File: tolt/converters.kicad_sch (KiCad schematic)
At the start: 50 parts, among them U14 AMS1117-3.3, U15 LP5907MFX-3.3, U16 TPS62173DSG, U19 TLV61047DDC, U24 LTC7138xMSE

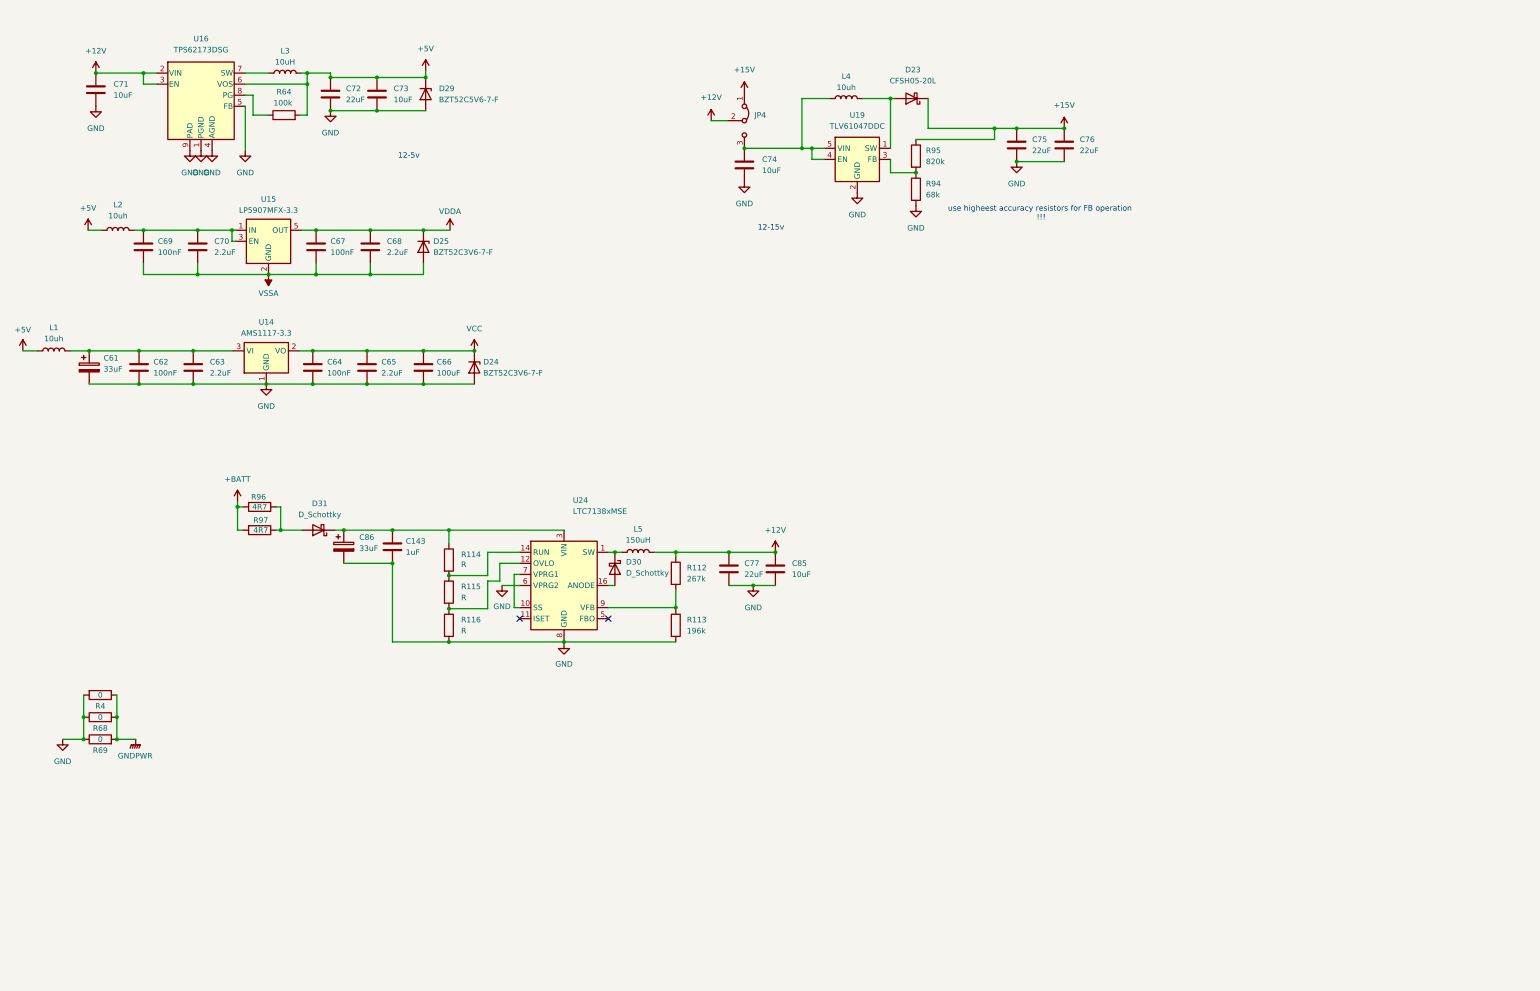
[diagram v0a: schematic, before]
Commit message: converter edit
2x ltc7137
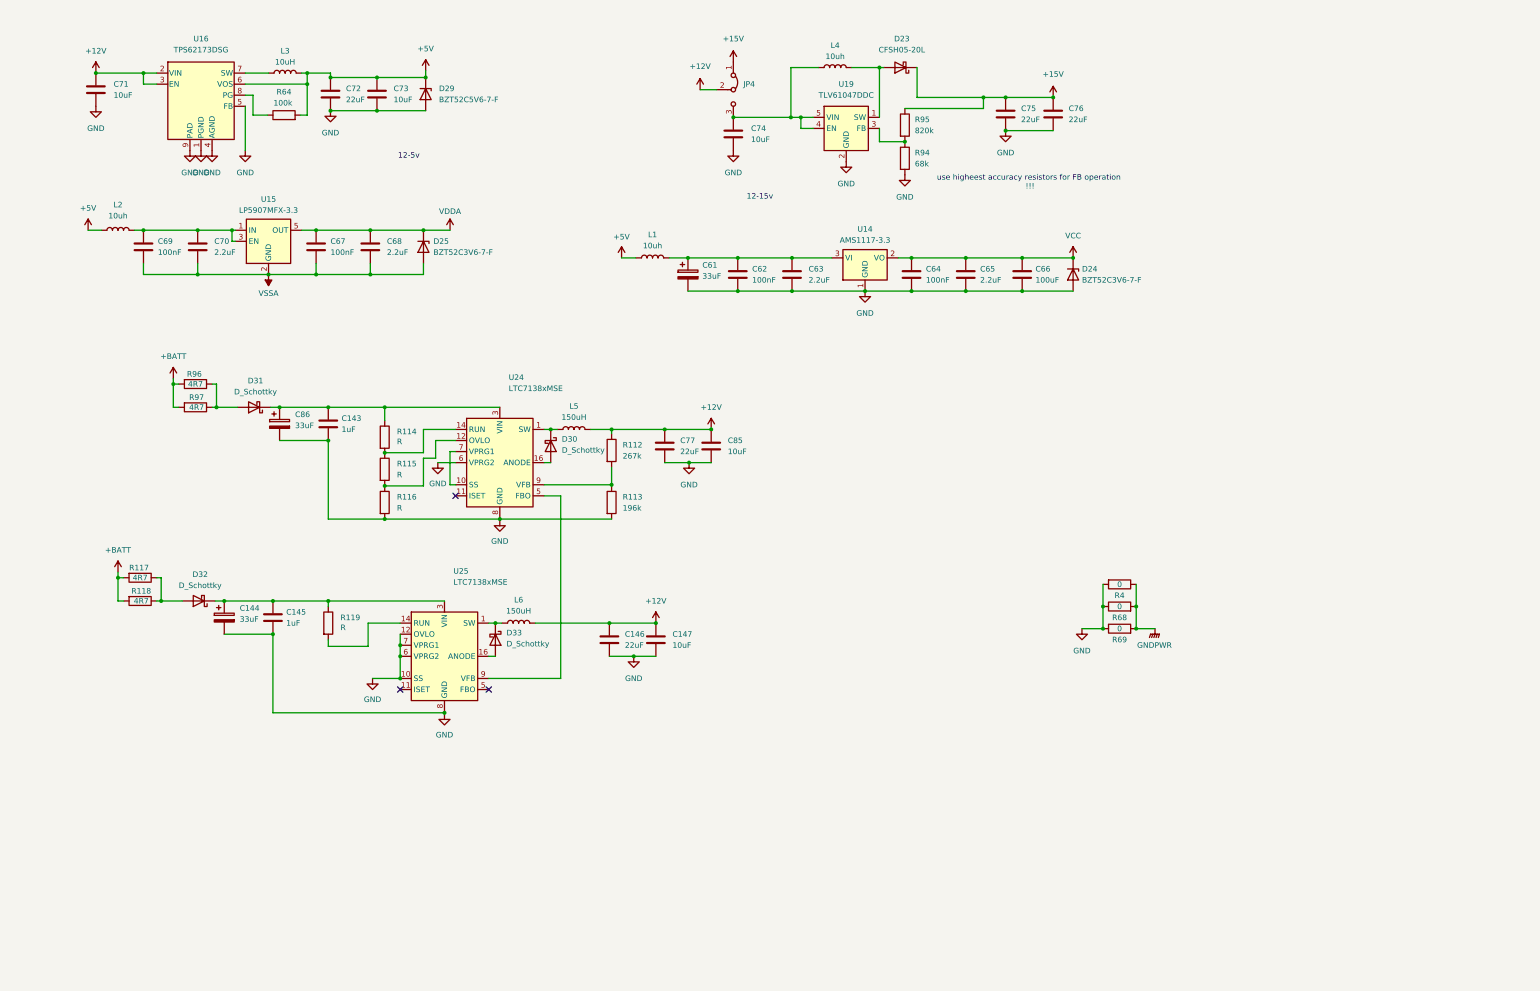
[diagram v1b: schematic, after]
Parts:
- added C144: 33uF, Capacitor_Tantalum_SMD:CP_EIA-3528-15_AVX-H, symbol Device:C_Polarized
- added C145: 1uF, Capacitor_SMD:C_2220_5750Metric, symbol Device:C
- added C146: 22uF, Capacitor_SMD:C_1210_3225Metric, symbol Device:C
- added C147: 10uF, Capacitor_SMD:C_1210_3225Metric, symbol Device:C
- added D32, D33: D_Schottky, symbol Device:D_Schottky
- added L6: 150uH, symbol Device:L
- added R117, R118: 4R7, Resistor_SMD:R_0805_2012Metric, symbol Device:R
- added R119: R, symbol Device:R
- added U25: LTC7138xMSE, Package_SO:Analog_MSOP-12-16-1EP_3x4.039mm_P0.5mm_EP1.651x2.845mm, symbol Regulator_Switching:LTC7138xMSE
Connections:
- net +12V: now also C146.2, C147.2, L6.2
- net +BATT: now also R117.2, R118.2
- net GND: now also C144.2, C145.2, C146.1, C147.1, U25.10 (SS), U25.12 (OVLO), U25.17 (GND), U25.6 (VPRG2), U25.7 (VPRG1), U25.8 (GND)
- net at U24.5 (FBO): now also U25.9 (VFB)
- new net: C144.1, C145.1, D32.1 (K), R119.1, U25.3 (VIN)
- new net: R119.2, U25.14 (RUN)
- new net: D32.2 (A), R117.1, R118.1
- new net: D33.1 (K), L6.1, U25.1 (SW)
- new net: D33.2 (A), U25.16 (ANODE)
- no-connect marks 2 -> 3
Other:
- moved on the sheet: C143, C61, C62, C63, C64, C65, C66, C74, C75, C76, C77, C85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

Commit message: more changes
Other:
- note added: "analog"
- note added: "consider using another converter for 15v ?"
- note added: "digital"
- note added: "dual 12v coneverter for 800ma output"
- moved on the sheet: R4, R68, R69
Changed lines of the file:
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@@
 		)
 	)
+	(text "analog\n"
+		(exclude_from_sim no)
+		(at 106.172 80.518 0)
+		(effects
+			(font
+				(size 1.27 1.27)
+			)
+		)
+	)
+	(text "consider using another converter for 15v ?"
+		(exclude_from_sim no)
+		(at 253.746 48.768 0)
+		(effects
+			(font
+				(size 1.27 1.27)
+			)
+		)
+	)
+	(text "dual 12v coneverter for 800ma output \n"
+		(exclude_from_sim no)
+		(at 149.606 183.134 0)
+		(effects
+			(font
+				(size 1.27 1.27)
+			)
+		)
+	)
 	(text "12-5v\n"
 		(exclude_from_sim no)
@@
 		)
 	)
+	(text "digital\n"
+		(exclude_from_sim no)
+		(at 259.588 84.836 0)
+		(effects
+			(font
+				(size 1.27 1.27)
+			)
+		)
+	)
 	(junction
 		(at 222.758 69.85)
@@
 	)
 	(junction
-		(at 266.7 149.86)
+		(at 241.3 127)
 		(diameter 0)
 		(color 0 0 0 0)
@@
 	)
 	(junction
-		(at 274.32 154.94)
+		(at 248.92 132.08)
 		(diameter 0)
 		(color 0 0 0 0)
@@
 	)
 	(junction
-		(at 274.32 149.86)
+		(at 248.92 127)
 		(diameter 0)
 		(color 0 0 0 0)
 	)
 	(junction
-		(at 266.7 154.94)
+		(at 241.3 132.08)
 		(diameter 0)
 		(color 0 0 0 0)
@@
 	(wire
 		(pts
-			(xy 274.32 149.86) (xy 274.32 154.94)
+			(xy 248.92 127) (xy 248.92 132.08)
 		)
 		(stroke
@@
 	(wire
 		(pts
-			(xy 274.32 144.78) (xy 274.32 149.86)
+			(xy 248.92 121.92) (xy 248.92 127)
 		)
 		(stroke
@@
 	(wire
 		(pts
-			(xy 266.7 149.86) (xy 266.7 154.94)
+			(xy 241.3 127) (xy 241.3 132.08)
 		)
 		(stroke
@@
 	(wire
 		(pts
-			(xy 261.874 154.94) (xy 266.7 154.94)
+			(xy 236.474 132.08) (xy 241.3 132.08)
 		)
 		(stroke
@@
 	(wire
 		(pts
-			(xy 274.32 154.94) (xy 278.638 154.94)
+			(xy 248.92 132.08) (xy 253.238 132.08)
 		)
 		(stroke
@@
 	(wire
 		(pts
-			(xy 266.7 144.78) (xy 266.7 149.86)
+			(xy 241.3 121.92) (xy 241.3 127)
 		)
 		(stroke
@@
 	(symbol
 		(lib_id "power:GNDPWR")
-		(at 278.638 154.94 0)
+		(at 253.238 132.08 0)
 		(unit 1)
 		(exclude_from_sim no)
@@
 		(fields_autoplaced yes)
 		(property "Reference" "#PWR0217"
-			(at 278.638 160.02 0)
+			(at 253.238 137.16 0)
 			(effects
 				(font
@@
 		)
 		(property "Value" "GNDPWR"
-			(at 278.511 158.75 0)
+			(at 253.111 135.89 0)
 			(effects
 				(font
@@
 		)
 		(property "Footprint" ""
-			(at 278.638 156.21 0)
+			(at 253.238 133.35 0)
 			(effects
 				(font
@@
 		)
 		(property "Datasheet" ""
-			(at 278.638 156.21 0)
+			(at 253.238 133.35 0)
 			(effects
 				(font
@@
 		)
 		(property "Description" "Power symbol creates a global label with name \"GNDPWR\" , global ground"
-			(at 278.638 154.94 0)
+			(at 253.238 132.08 0)
 			(effects
 				(font
@@
 	(symbol
 		(lib_id "Device:R")
-		(at 270.51 149.86 90)
+		(at 245.11 127 90)
 		(unit 1)
 		(exclude_from_sim no)
@@
 		(dnp no)
 		(property "Reference" "R68"
-			(at 270.51 152.4 90)
+			(at 245.11 129.54 90)
 			(effects
 				(font
@@
 		)
 		(property "Value" "0"
-			(at 270.51 149.86 90)
+			(at 245.11 127 90)
 			(effects
 				(font
@@
 		)
 		(property "Footprint" "Resistor_SMD:R_0815_2038Metric"
-			(at 270.51 151.638 90)
+			(at 245.11 128.778 90)
 			(effects
 				(font
@@
 		)
 		(property "Datasheet" "~"
-			(at 270.51 149.86 0)
+			(at 245.11 127 0)
 			(effects
 				(font
@@
 		)
 		(property "Description" "Resistor"
-			(at 270.51 149.86 0)
+			(at 245.11 127 0)
 			(effects
 				(font
@@
 	(symbol
 		(lib_id "power:GND")
-		(at 261.874 154.94 0)
+		(at 236.474 132.08 0)
 		(unit 1)
 		(exclude_from_sim no)
@@
 		(fields_autoplaced yes)
 		(property "Reference" "#PWR0218"
-			(at 261.874 161.29 0)
+			(at 236.474 138.43 0)
 			(effects
 				(font
@@
 		)
 		(property "Value" "GND"
-			(at 261.874 160.02 0)
+			(at 236.474 137.16 0)
 			(effects
 				(font
@@
 		)
 		(property "Footprint" ""
-			(at 261.874 154.94 0)
+			(at 236.474 132.08 0)
 			(effects
 				(font
@@
 		)
 		(property "Datasheet" ""
-			(at 261.874 154.94 0)
+			(at 236.474 132.08 0)
 			(effects
 				(font
@@
 		)
 		(property "Description" ""
-			(at 261.874 154.94 0)
+			(at 236.474 132.08 0)
 			(effects
 				(font
@@
 	(symbol
 		(lib_id "Device:R")
-		(at 270.51 144.78 270)
+		(at 245.11 121.92 270)
 		(unit 1)
 		(exclude_from_sim no)
@@
 		(dnp no)
 		(property "Reference" "R4"
-			(at 270.51 147.32 90)
+			(at 245.11 124.46 90)
 			(effects
 				(font
@@
 		)
 		(property "Value" "0"
-			(at 270.51 144.78 90)
+			(at 245.11 121.92 90)
 			(effects
 				(font
@@
 		)
 		(property "Footprint" "Resistor_SMD:R_0815_2038Metric"
-			(at 270.51 143.002 90)
+			(at 245.11 120.142 90)
 			(effects
 				(font
@@
 		)
 		(property "Datasheet" "~"
-			(at 270.51 144.78 0)
+			(at 245.11 121.92 0)
 			(effects
 				(font
@@
 		)
 		(property "Description" ""
-			(at 270.51 144.78 0)
+			(at 245.11 121.92 0)
 			(effects
 				(font
@@
 	(symbol
 		(lib_id "Device:R")
-		(at 270.51 154.94 90)
+		(at 245.11 132.08 90)
 		(unit 1)
 		(exclude_from_sim no)
@@
 		(dnp no)
 		(property "Reference" "R69"
-			(at 270.51 157.48 90)
+			(at 245.11 134.62 90)
 			(effects
 				(font
@@
 		)
 		(property "Value" "0"
-			(at 270.51 154.94 90)
+			(at 245.11 132.08 90)
 			(effects
 				(font
@@
 		)
 		(property "Footprint" "Resistor_SMD:R_0815_2038Metric"
-			(at 270.51 156.718 90)
+			(at 245.11 133.858 90)
 			(effects
 				(font
@@
 		)
 		(property "Datasheet" "~"
-			(at 270.51 154.94 0)
+			(at 245.11 132.08 0)
 			(effects
 				(font
@@
 		)
 		(property "Description" "Resistor"
-			(at 270.51 154.94 0)
+			(at 245.11 132.08 0)
 			(effects
 				(font

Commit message: ltc
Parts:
- removed R117, R118, R96, R97: 4R7, Resistor_SMD:R_0805_2012Metric, symbol Device:R
- D30, D31, D32, D33: footprint (none) -> Diode_SMD:D_2512_6332Metric
- L5, L6: footprint (none) -> Library:IND-SMD_L5.0-W5.0
- R112, R113, R114, R115, R116, R119: footprint (none) -> Resistor_SMD:R_0603_1608Metric
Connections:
- net +BATT: now also D31.2 (A), D32.2 (A)

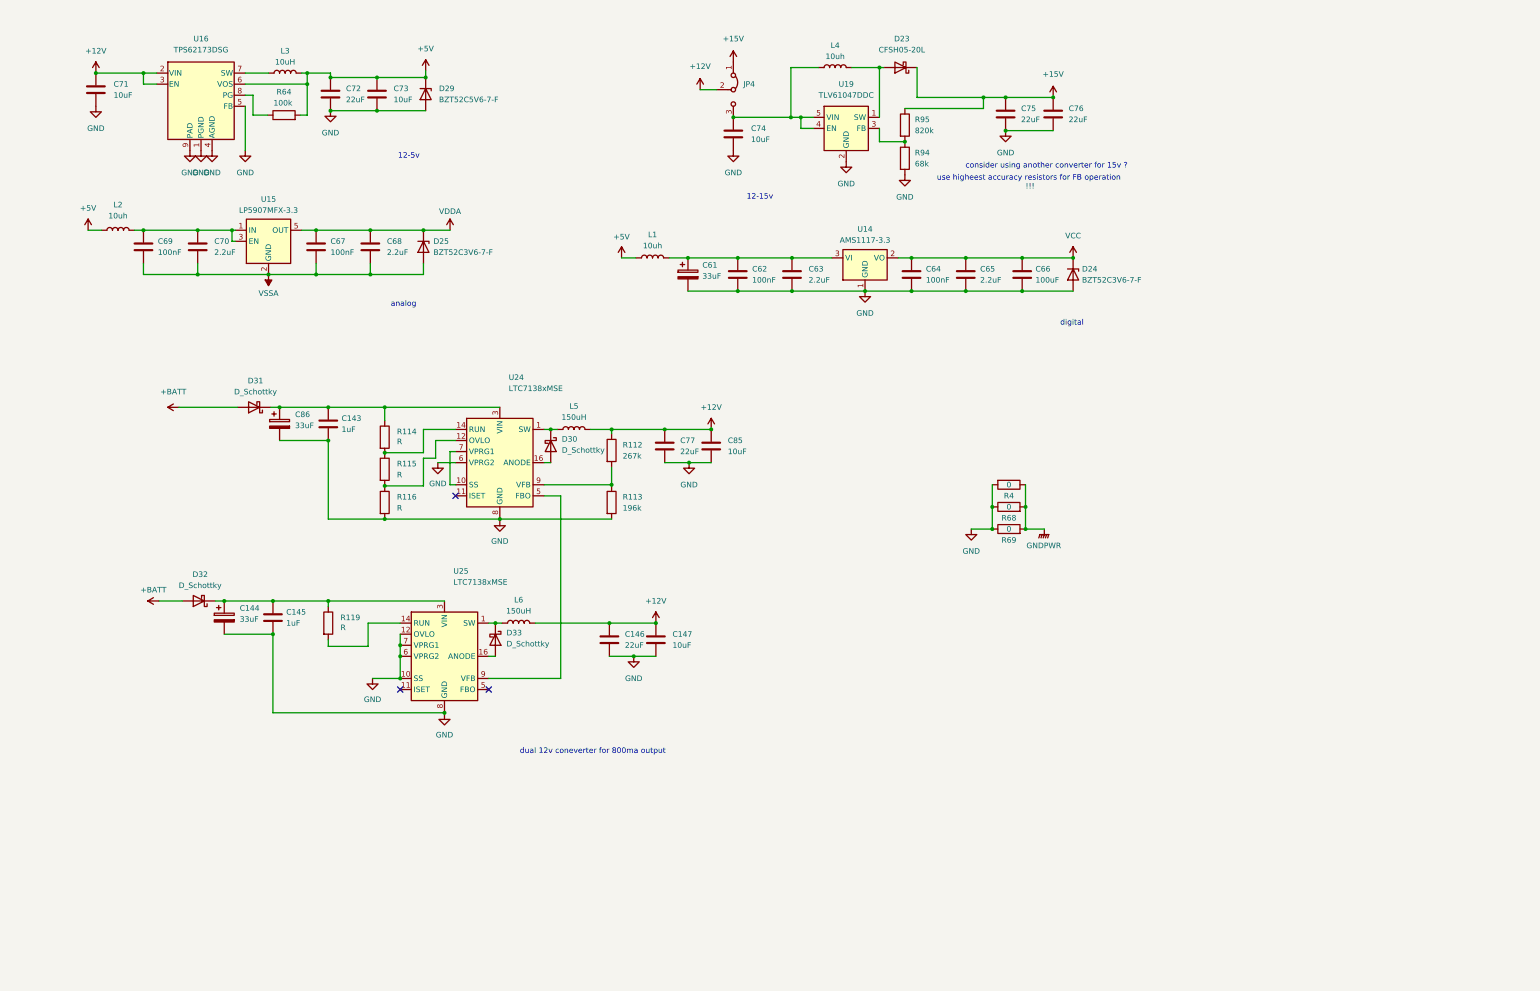
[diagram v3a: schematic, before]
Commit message: modified:   tolt/converters.kicad_sch 	modified:   tolt/tolt.kicad_pcb
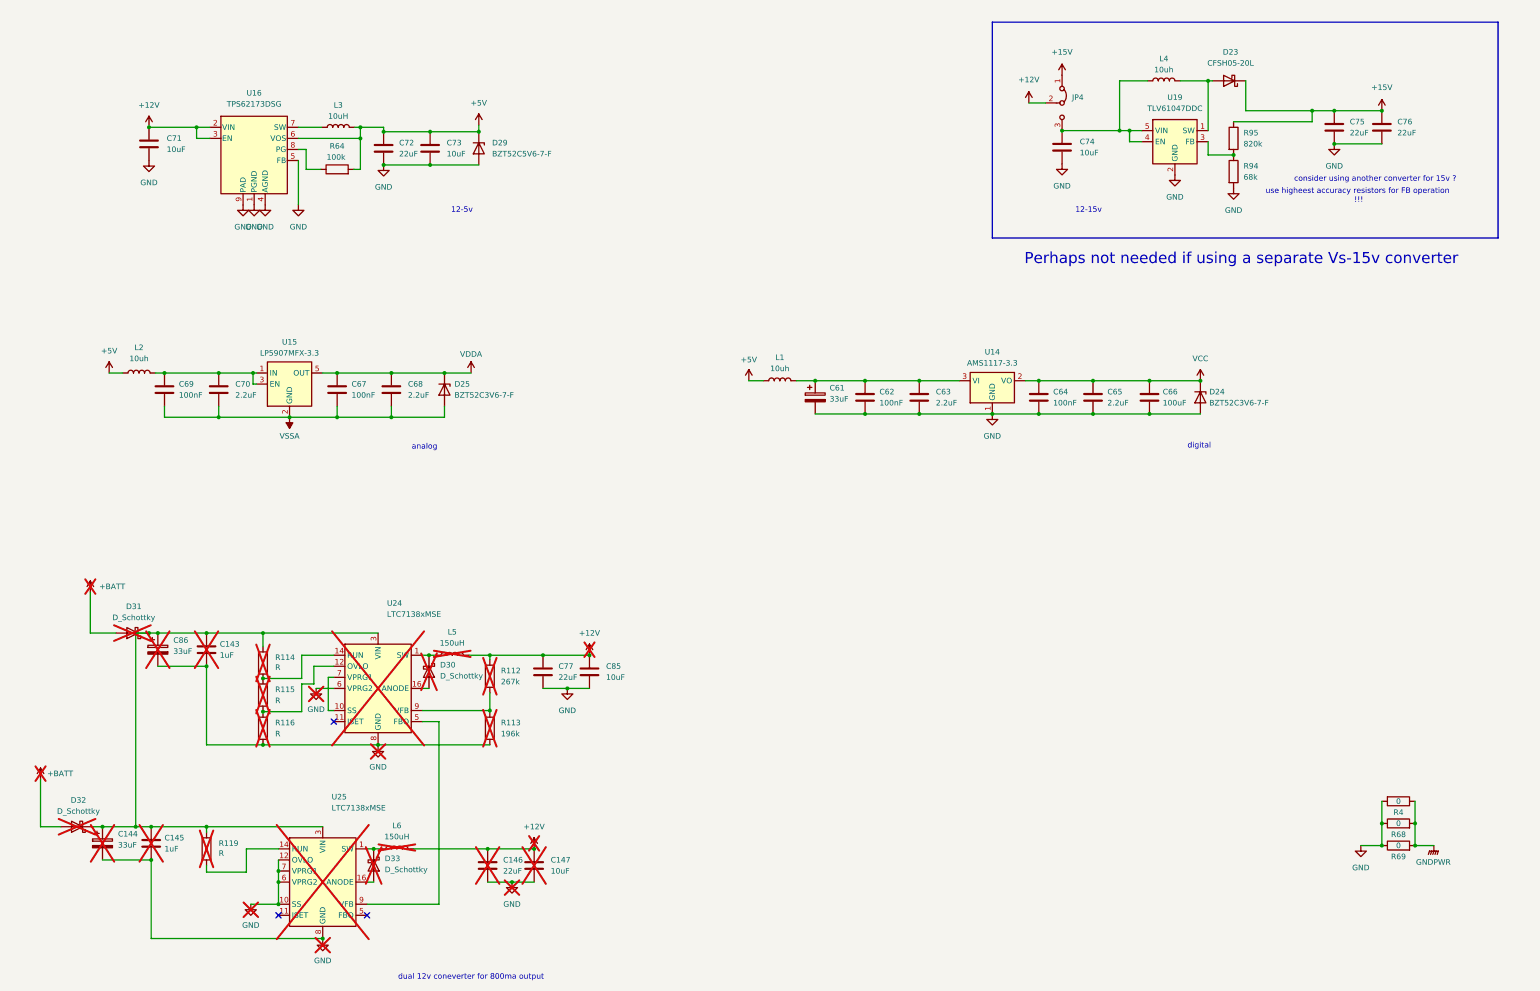
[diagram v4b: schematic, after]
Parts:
- C143, C144, C145, C146, C147, C86, D30, D31, D32, D33, L5, L6, R112, R113, R114, R115, R116, R119, U24, U25: now not fitted
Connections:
- net at C144.1, C145.1, D32.1 (K)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: now also C143.1, C86.1, D31.1 (K), R114.1, U24.3 (VIN)
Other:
- note added: "Perhaps not needed if using a separate Vs-15v converter"
- moved on the sheet: C61, C62, C63, C64, C65, C66, C67, C68, C69, C70, C71, C72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

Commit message: modified:   tolt/auxl.kicad_sch 	modified:   tolt/converters.kicad_sch 	modified:   tolt/tolt.kicad_pcb
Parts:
- removed C144: 33uF, Capacitor_Tantalum_SMD:CP_EIA-3528-15_AVX-H, symbol Device:C_Polarized
- removed C145: 1uF, Capacitor_SMD:C_2220_5750Metric, symbol Device:C
- removed C146: 22uF, Capacitor_SMD:C_1210_3225Metric, symbol Device:C
- removed C147: 10uF, Capacitor_SMD:C_1210_3225Metric, symbol Device:C
- removed D33: D_Schottky, Diode_SMD:D_2512_6332Metric, symbol Device:D_Schottky
- removed L6: 150uH, Library:IND-SMD_L5.0-W5.0, symbol Device:L
- removed R119: R, Resistor_SMD:R_0603_1608Metric, symbol Device:R
- removed U25: LTC7138xMSE, Package_SO:Analog_MSOP-12-16-1EP_3x4.039mm_P0.5mm_EP1.651x2.845mm, symbol Regulator_Switching:LTC7138xMSE
- added C148: 22uF, Capacitor_SMD:C_1210_3225Metric, symbol Device:C
- added C149: 10uF, Capacitor_SMD:C_1210_3225Metric, symbol Device:C
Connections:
- net +12V: now also C148.2, C149.2
- net GND: now also C148.1, C149.1
- no-connect marks 3 -> 2
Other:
- note removed: "dual 12v coneverter for 800ma output"
- moved on the sheet: D32
